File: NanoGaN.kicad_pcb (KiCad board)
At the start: 2 copper layers, 197 parts, among them J1 U_DC, J10 Conn_01x06, J11 Conn_01x04, J12 USB4085-GF-A, J13 Conn_01x02, J2 GND, J3 Phase_U, J4 Phase_V, J5 Phase_W, J6 FTSH-107-01-L-DV-K-TR, J7 Conn_01x03, J8 Conn_01x02, J9 Conn_01x07, Q1 IGC025S08S1, Q2 IGC025S08S1, Q3 IGC025S08S1, Q4 IGC025S08S1, Q5 IGC025S08S1, Q6 IGC025S08S1, Q7 Si2302CDS, U1 STM32H723VGTx, U10 LMG1205YFXR, U10 SN74LVC1G66DCKR, U11 SN74LVC1G66DCKR, U12 AD8418, U12 LMG1205YFXR, U13 BMI323, U14 AS5047P-ATST, U15 TCAN1044VDRQ1, U16 SN74LVC1G66DCKR, U17 AD8418, U18 SN74LVC1G66DCKR, U2 LMR51635XDDCR, U3 AMS1117, U4 AD8418, U5 LMG1205YFXR, U6 SN74LVC1G66DCKR, U7 LMG1205YFXR, U7 SN74LVC1G66DCKR, U8 LMG1205YFXR, U9 AD8418, X1 8MHz

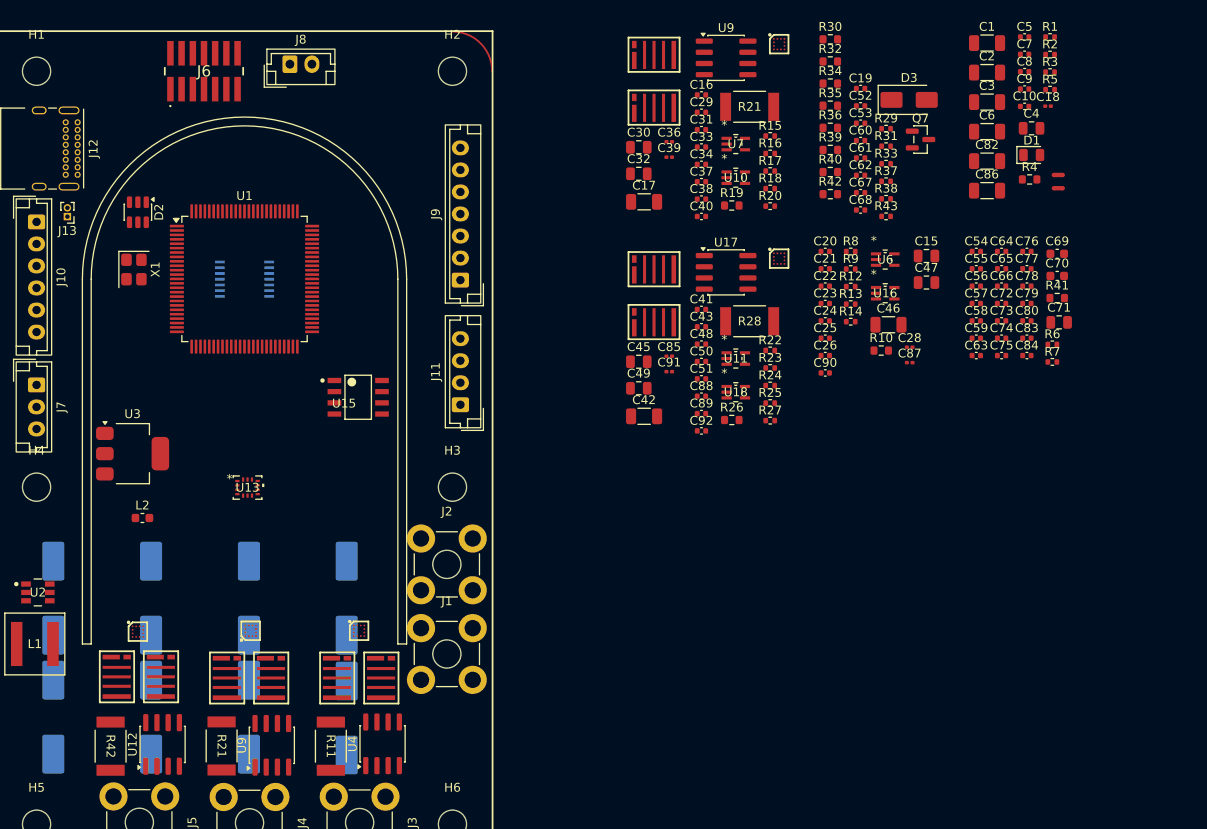
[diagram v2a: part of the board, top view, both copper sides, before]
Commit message: Differential pair naming added. Duplicate footprint problem fixed.
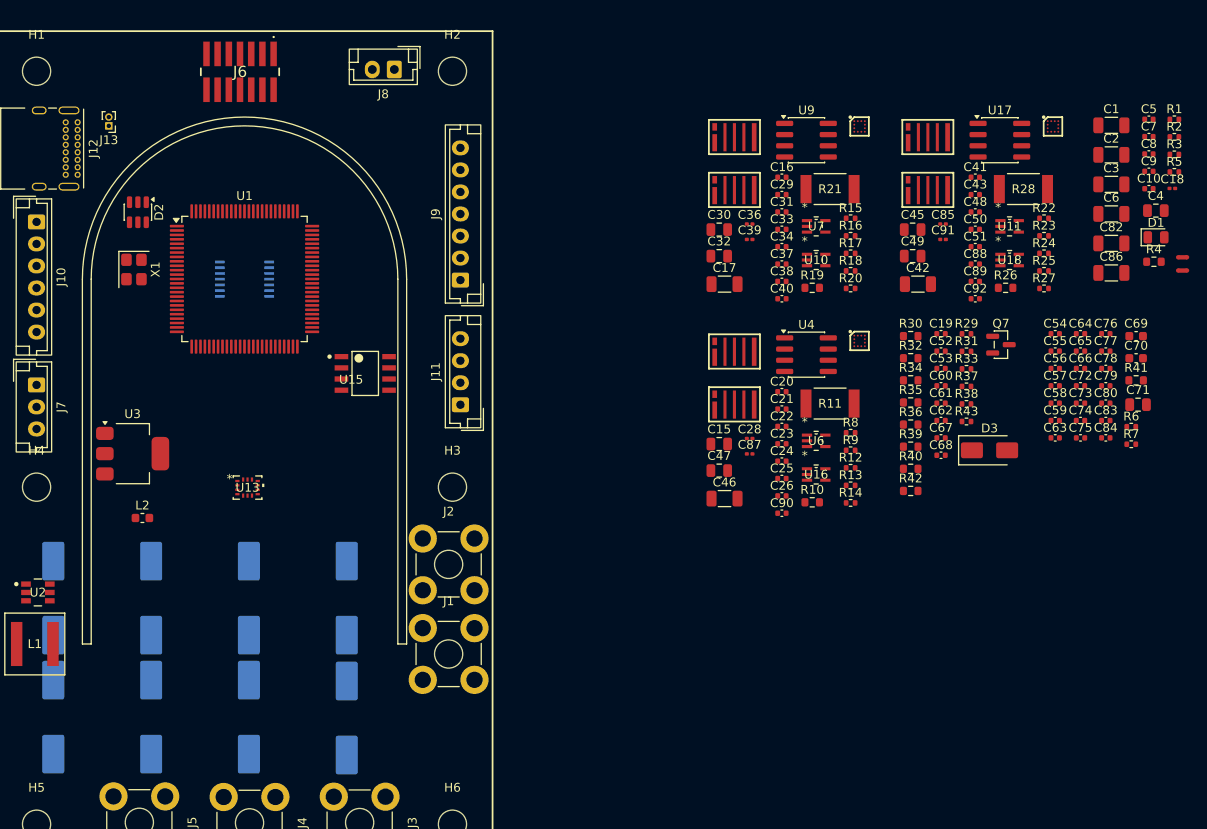
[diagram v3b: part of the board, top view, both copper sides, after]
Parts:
- removed the Q3 at (90.1, 17.9)
- removed the Q3 at (41.9, 88.9)
- removed the Q4 at (90.1, 23.9)
- removed the Q4 at (46.9, 88.9)
- removed the Q5 at (90.1, 42.2)
- removed the Q5 at (29.4, 88.7)
- removed the Q6 at (90.1, 48.2)
- removed the Q6 at (34.4, 88.7)
- removed the R21 at (41.0, 96.6)
- removed the R21 at (100.9, 24.0)
- removed the R42 at (28.4, 96.6)
- removed the R42 at (110.1, 34.0)
- removed the U10 at (31.5, 83.6)
- removed the U10 at (99.4, 32.1)
- removed the U12 at (34.3, 96.4)
- removed the U12 at (104.3, 41.3)
- removed the U7 at (99.4, 28.3)
- removed the U7 at (44.3, 83.5)
- removed the U9 at (46.7, 96.5)
- removed the U9 at (98.2, 18.5)
- added Q3: IGC025S08S1, NanoGaN:IFX-PG-TSON-6-2-V, F.Cu at (99.2, 27.2)
- added Q4: IGC025S08S1, NanoGaN:IFX-PG-TSON-6-2-V, F.Cu at (99.2, 33.2)
- added Q5: IGC025S08S1, NanoGaN:IFX-PG-TSON-6-2-V, F.Cu at (121.2, 27.2)
- added Q6: IGC025S08S1, NanoGaN:IFX-PG-TSON-6-2-V, F.Cu at (121.2, 33.2)
- added R21: 1m, NanoGaN:RES_00FEA_VIS-L, F.Cu at (110.1, 33.4)
- added R42: 10k, Resistor_SMD:R_0603_1608Metric, F.Cu at (119.2, 67.6)
- added U10: SN74LVC1G66DCKR, NanoGaN:DCK5, F.Cu at (108.5, 41.4)
- added U12: LMG1205YFXR, NanoGaN:BGA12C40P4X4_173X188X68, F.Cu at (135.3, 26.3)
- added U7: SN74LVC1G66DCKR, NanoGaN:DCK5, F.Cu at (108.5, 37.6)
- added U9: AD8418, Package_SO:SOIC-8_3.9x4.9mm_P1.27mm, F.Cu at (107.4, 27.8)
- moved R11 68.7 mm to (110.1, 57.7), turned to 0 degrees
- moved U5 65.6 mm to (113.4, 50.6)
- moved U4 65.3 mm to (107.4, 52.2), turned to 0 degrees
- moved Q1 58.3 mm to (99.2, 51.6), turned to 0 degrees
- moved Q2 50.7 mm to (99.2, 57.6), turned to 0 degrees
- moved D3 40.8 mm to (128.2, 63.0)
- moved R30 34.9 mm to (119.2, 50.1)
- moved R35 34.9 mm to (119.2, 57.6)
- moved R40 34.9 mm to (119.2, 65.1)
- moved R32 34.9 mm to (119.2, 52.6)
- moved R34 34.9 mm to (119.2, 55.1)
- moved R36 34.9 mm to (119.2, 60.1)
- moved R39 34.9 mm to (119.2, 62.6)
- moved C41 34.5 mm to (126.5, 32.0)
- moved C42 34.5 mm to (120.0, 44.2)
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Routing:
- net /Connectors/SPI3_NSS: track 0.00 -> 0.62 mm
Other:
- copper layers 2 -> 6

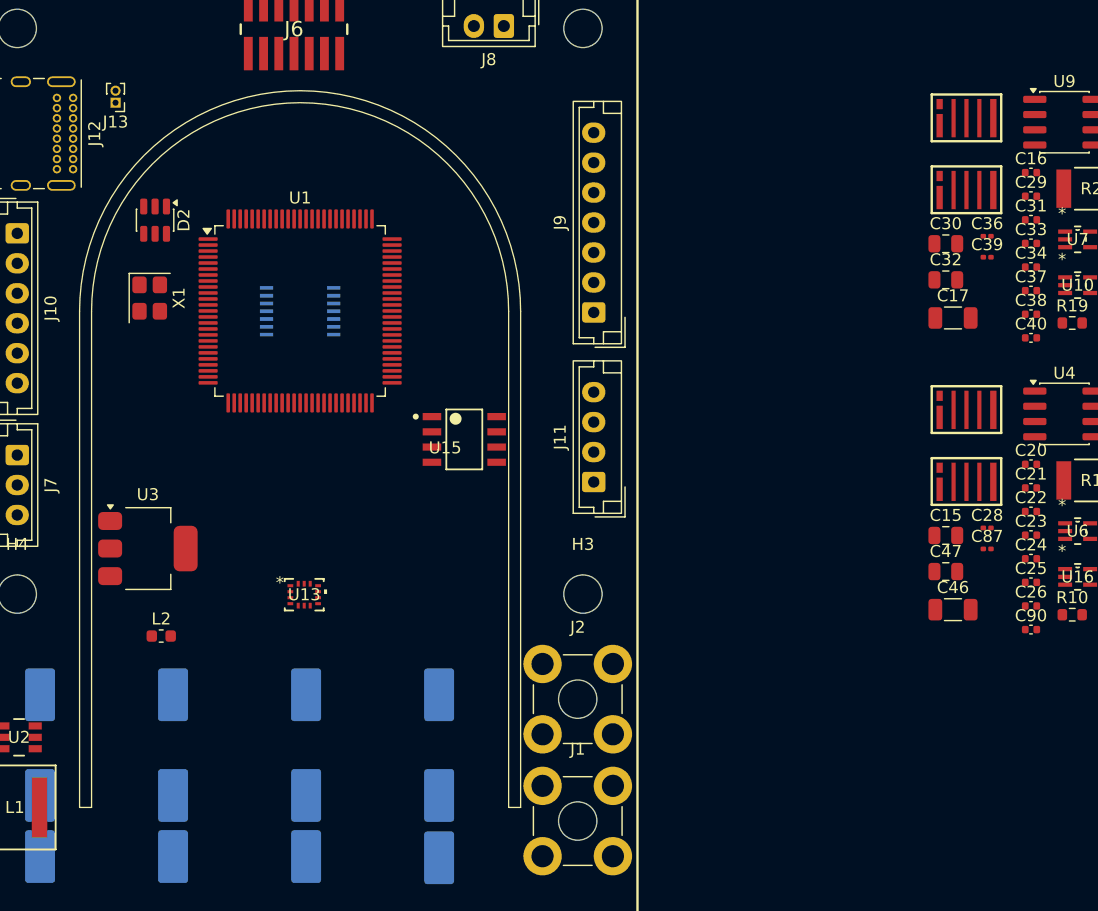
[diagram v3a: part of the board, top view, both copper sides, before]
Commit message: added Net Classes  added +5V supply selection header
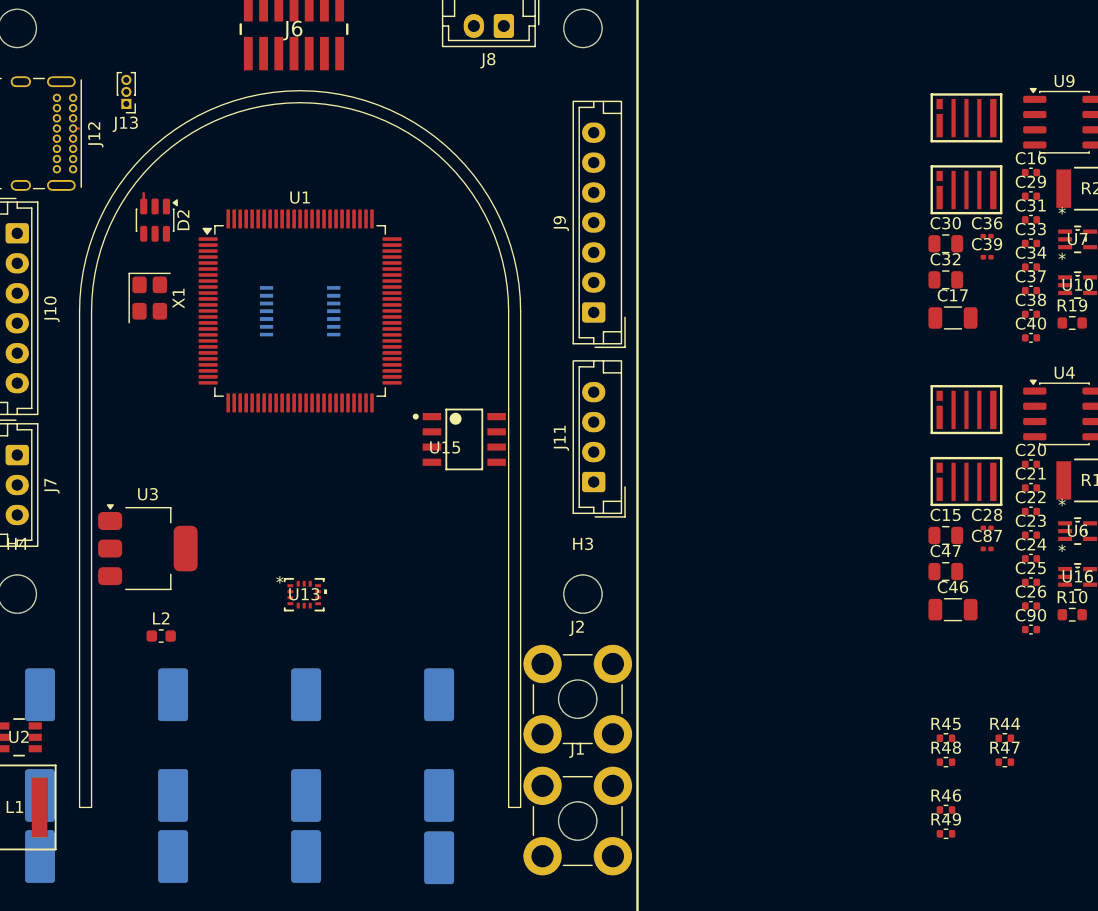
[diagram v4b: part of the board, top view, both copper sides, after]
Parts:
- added R44: 0, Resistor_SMD:R_0402_1005Metric, F.Cu at (102.4, 79.2)
- added R45: 0, Resistor_SMD:R_0402_1005Metric, F.Cu at (97.5, 79.2)
- added R46: 0, Resistor_SMD:R_0402_1005Metric, F.Cu at (97.5, 85.2)
- added R47: 0, Resistor_SMD:R_0402_1005Metric, F.Cu at (102.4, 81.2)
- added R48: 0, Resistor_SMD:R_0402_1005Metric, F.Cu at (97.5, 81.2)
- added R49: 0, Resistor_SMD:R_0402_1005Metric, F.Cu at (97.5, 87.2)
- J13: value Conn_01x02 -> Conn_01x03; footprint Connector_PinHeader_1.00mm:PinHeader_1x02_P1.00mm_Vertical -> Connector_PinHeader_1.00mm:PinHeader_1x03_P1.00mm_Vertical
- moved J13 0.91 mm to (29.1, 26.3)
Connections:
- net /Connectors/CANH renamed /MCU/CAN+
- net /Connectors/CANL renamed /MCU/CAN-
- net /Connectors/D+ renamed /Connectors/USBD+
- net /Connectors/D- renamed /Connectors/USBD-
- net Net-(C83-Pad1) renamed /MCU/VCAP1
- net Net-(C84-Pad1) renamed /MCU/VCAP2
- net Net-(D3-A) renamed /Connectors/FANN
- net Net-(J12-CC1) renamed /Connectors/USBCC1
- net Net-(J12-CC2) renamed /Connectors/USBCC2
- net Net-(U1-PH0) renamed /MCU/HSE_IN
- net Net-(U1-PH1) renamed /MCU/HSE_OUT
- net Net-(U12-HB) renamed /HalfBridgeW/HB
- net Net-(U5-HB) renamed /HalfBridgeU/HB
- net Net-(U8-HB) renamed /HalfBridgeV/HB
- C6 pad 1: +5V -> +5V_SMPS
- C67 pad 1: Net-(D2-VBUS) -> /Connectors/USBVBUS
- C68 pad 1: Net-(J13-Pin_2) -> +5V_USB
- C82 pad 1: +5V -> +5V_SMPS
- C86 pad 1: +5V -> +5V_SMPS
- D2 pad 5: Net-(D2-VBUS) -> /Connectors/USBVBUS
- J12 pad A4: Net-(D2-VBUS) -> /Connectors/USBVBUS
- J12 pad A9: Net-(D2-VBUS) -> /Connectors/USBVBUS
- J12 pad B4: Net-(D2-VBUS) -> /Connectors/USBVBUS
- J12 pad B9: Net-(D2-VBUS) -> /Connectors/USBVBUS
- J13 pad 1: Net-(D2-VBUS) -> +5V_USB
- J13 pad 2: Net-(J13-Pin_2) -> +5V
- L1 pad 2: +5V -> +5V_SMPS
- Q1 pad 1: /HalfBridgeU/HOL -> /HalfBridgeU/HIGH_GATE
- Q2 pad 1: /HalfBridgeU/LOL -> /HalfBridgeU/LOW_GATE
- Q3 pad 1: /HalfBridgeV/HOL -> /HalfBridgeV/HIGH_GATE
- Q4 pad 1: /HalfBridgeV/LOL -> /HalfBridgeV/LOW_GATE
- Q5 pad 1: /HalfBridgeW/HOL -> /HalfBridgeW/HIGH_GATE
- Q6 pad 1: /HalfBridgeW/LOL -> /HalfBridgeW/LOW_GATE
- R1 pad 1: +5V -> +5V_SMPS
- R13 pad 1: /HalfBridgeU/HOL -> /HalfBridgeU/HIGH_GATE
- R14 pad 1: /HalfBridgeU/LOL -> /HalfBridgeU/LOW_GATE
- R15 pad 2: /HalfBridgeV/HOL -> /HalfBridgeV/HIGH_GATE
- R16 pad 2: /HalfBridgeV/LOL -> /HalfBridgeV/LOW_GATE
- R17 pad 1: /HalfBridgeV/HOL -> /HalfBridgeV/HIGH_GATE
- R18 pad 1: /HalfBridgeV/LOL -> /HalfBridgeV/LOW_GATE
- R22 pad 2: /HalfBridgeW/HOL -> /HalfBridgeW/HIGH_GATE
- R23 pad 2: /HalfBridgeW/LOL -> /HalfBridgeW/LOW_GATE
- R24 pad 1: /HalfBridgeW/HOL -> /HalfBridgeW/HIGH_GATE
- R25 pad 1: /HalfBridgeW/LOL -> /HalfBridgeW/LOW_GATE
- R39 pad 1: Net-(D2-VBUS) -> /Connectors/USBVBUS
- R39 pad 2: Net-(J13-Pin_2) -> +5V_USB
- R40 pad 1: Net-(D2-VBUS) -> /Connectors/USBVBUS
- R8 pad 2: /HalfBridgeU/HOL -> /HalfBridgeU/HIGH_GATE
- R9 pad 2: /HalfBridgeU/LOL -> /HalfBridgeU/LOW_GATE
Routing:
- net /Connectors/USBD+: track 0.00 -> 1.61 mm

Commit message: WiP layout
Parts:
- removed H1, H2, H3, H4, H5, H6: MountingHole, MountingHole:MountingHole_3.2mm_M3
- added C93: 1u, Capacitor_SMD:C_0402_1005Metric, F.Cu at (134.8, 77.8)
- added FM1: Fiducial, Fiducial:Fiducial_1mm_Mask2mm, F.Cu at (233.9, 108.7)
- added FM2: Fiducial, Fiducial:Fiducial_1mm_Mask2mm, F.Cu at (233.9, 112.2)
- added FM3: Fiducial, Fiducial:Fiducial_1mm_Mask2mm, F.Cu at (233.9, 115.8)
- added J14: Conn_01x03, Connector:FanPinHeader_1x03_P2.54mm_Vertical, F.Cu at (131.2, 53.0)
- added MH1: M2, MountingHole:MountingHole_2.2mm_M2_Pad_Via, F.Cu at (121.6, 51.4)
- added MH2: M2, MountingHole:MountingHole_2.2mm_M2_Pad_Via, F.Cu at (168.8, 51.4)
- added MH3: M2, MountingHole:MountingHole_2.2mm_M2_Pad_Via, F.Cu at (121.6, 98.6)
- added MH4: M2, MountingHole:MountingHole_2.2mm_M2_Pad_Via, F.Cu at (168.8, 98.6)
- added MH5: M2, MountingHole:MountingHole_2.2mm_M2_Pad_Via, F.Cu at (121.6, 138.6)
- added MH6: M2, MountingHole:MountingHole_2.2mm_M2_Pad_Via, F.Cu at (168.8, 138.6)
- added R50: 100, Resistor_SMD:R_0402_1005Metric, F.Cu at (134.2, 57.4)
- C58, C59: moved to B.Cu
- C69, C70: footprint Capacitor_SMD:C_0603_1608Metric -> Capacitor_SMD:C_0402_1005Metric
- C71: value 10u -> 4u7; footprint Capacitor_SMD:C_0805_2012Metric -> Capacitor_SMD:C_0402_1005Metric
- C72: value 1u -> 100n
- C79: value 100n -> 1u
- R34, R35, R36, R41, R42: footprint Resistor_SMD:R_0603_1608Metric -> Resistor_SMD:R_0402_1005Metric
- R7: value 0 -> 10k
- moved L2 160.3 mm to (190.7, 93.5)
- moved J12 153.1 mm to (165.2, 86.5), turned to 90 degrees
- moved J13 143.3 mm to (159.0, 86.8), turned to 0 degrees
- moved U2 140.6 mm to (158.9, 102.2), turned to 90 degrees
- moved L1 139.5 mm to (158.9, 96.2), turned to 90 degrees
- moved D2 136.5 mm to (160.2, 81.5), turned to 0 degrees
- moved U3 122.4 mm to (150.4, 90.0), turned to 180 degrees
- moved C10 117.0 mm to (262.5, 46.8)
- moved C15 117.0 mm to (213.7, 75.8)
- moved C30 117.0 mm to (213.7, 51.5)
- moved C32 117.0 mm to (213.7, 54.5)
- moved C41 117.0 mm to (242.8, 45.5)
- moved C43 117.0 mm to (242.8, 47.5)
- moved C47 117.0 mm to (213.7, 78.8)
- moved C48 117.0 mm to (242.8, 49.5)
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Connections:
- net Net-(J10-Pin_3) renamed /Connectors/HALL_IN1
- net Net-(J10-Pin_4) renamed /Connectors/HALL_IN2
- net Net-(J10-Pin_5) renamed /Connectors/HALL_IN3
- net Net-(U2-CB) renamed /Power/SW_CB
- net Net-(U2-FB) renamed /Power/SW_FB
- net Net-(U2-SW) renamed /Power/SW_SMPS
- C72 pad 1: +3V3 -> +3V3A
- C72 pad 2: GND -> AGND
- Q7 pad 2: Net-(Q7-G) -> /Connectors/FAN_Q_GATE
- R42 pad 1: Net-(Q7-G) -> GND
- R42 pad 2: GND -> /Connectors/FAN_Q_GATE
- R43 pad 1: Net-(Q7-G) -> /Connectors/FAN_Q_GATE
- R7 pad 1: GND -> FDCAN1_STB
- R7 pad 2: FDCAN3_STB -> GND
- U1 pad 58: FDCAN3_STB -> unconnected-(U1-PD11-Pad58)
- U1 pad 59: FDCAN3_RX -> unconnected-(U1-PD12-Pad59)
- U1 pad 60: FDCAN3_TX -> unconnected-(U1-PD13-Pad60)
- U1 pad 81: unconnected-(U1-PD0-Pad81) -> FDCAN1_RX
- U1 pad 82: unconnected-(U1-PD1-Pad82) -> FDCAN1_TX
- U1 pad 83: unconnected-(U1-PD2-Pad83) -> FDCAN1_STB
- U1 pad 90: unconnected-(U1-PB4(NJTRST)-Pad90) -> /Connectors/SERVO
- U1 pad 91: unconnected-(U1-PB5-Pad91) -> /Connectors/SERVO
- U1 pad 96: unconnected-(U1-PB9-Pad96) -> /Connectors/FAN_PWM
- U13 pad 1: SPI2_MISO -> SPI4_MISO
- U13 pad 12: SPI2_NSS -> SPI4_NSS
- U13 pad 13: SPI2_SCK -> SPI4_SCK
- U13 pad 14: SPI2_MOSI -> SPI4_MOSI
- U14 pad 1: SPI4_NSS -> SPI2_NSS
- U14 pad 2: SPI4_SCK -> SPI2_SCK
- U14 pad 3: SPI4_MISO -> SPI2_MISO
- U14 pad 4: SPI4_MOSI -> SPI2_MOSI
- U15 pad 1: FDCAN3_TX -> FDCAN1_TX
- U15 pad 4: FDCAN3_RX -> FDCAN1_RX
- U15 pad 8: FDCAN3_STB -> FDCAN1_STB
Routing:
- net /Connectors/USBD+: track 1.61 -> 0.35 mm
- net /Connectors/SPI3_NSS: track 0.62 -> 0.00 mm
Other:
- board outline added: 54 x 94 mm
- rule pad_to_mask_clearance: 0 -> 0.1
- board text removed: "${REFERENCE}"
